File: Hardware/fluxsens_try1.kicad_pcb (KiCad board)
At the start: 2 copper layers, 48.3 x 30.5 mm, 29 parts, among them J1 Conn_Coaxial, J2 Conn_Coaxial, J3 Conn_01x03, U1 DRV5033AJQDBZ, U3 DRV5033AJQDBZ, U5 DRV5033AJQDBZ, U6 DRV5033AJQDBZ

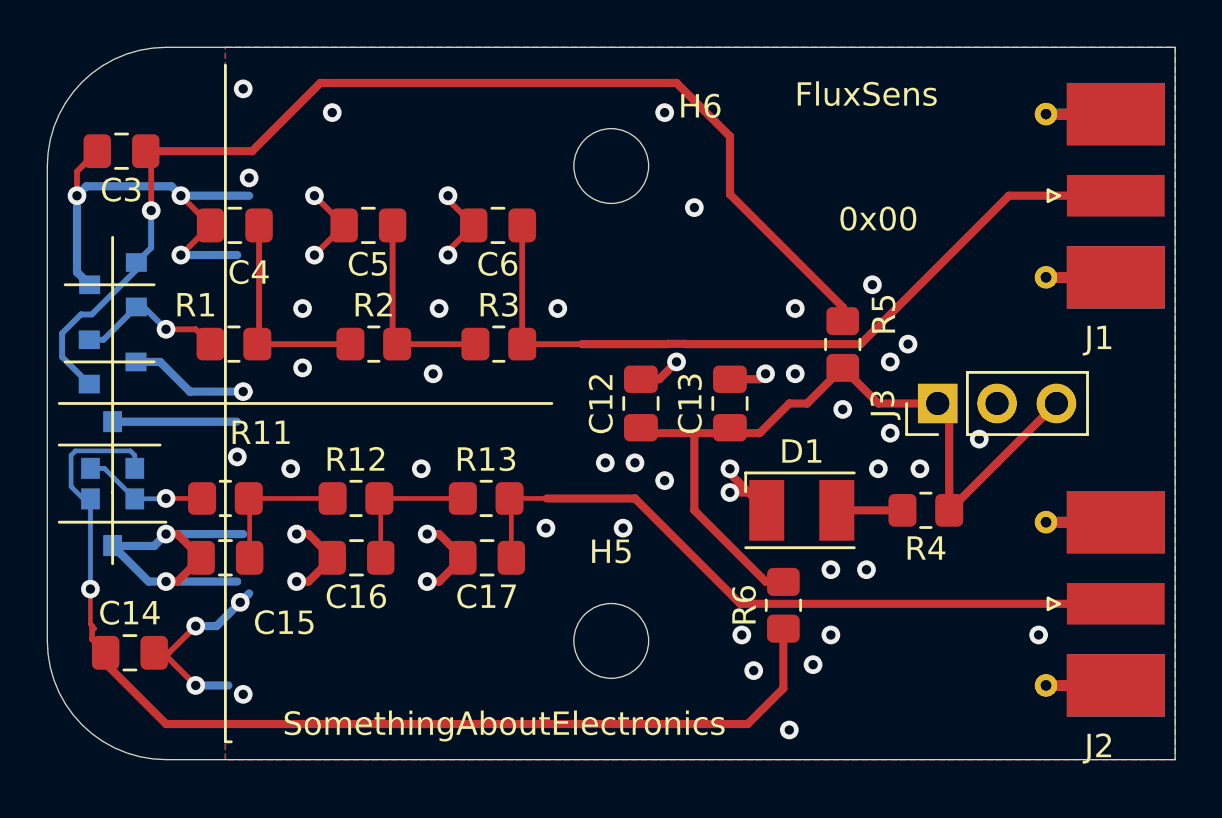
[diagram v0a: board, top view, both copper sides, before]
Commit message: changeover from Kicad V5 to V6
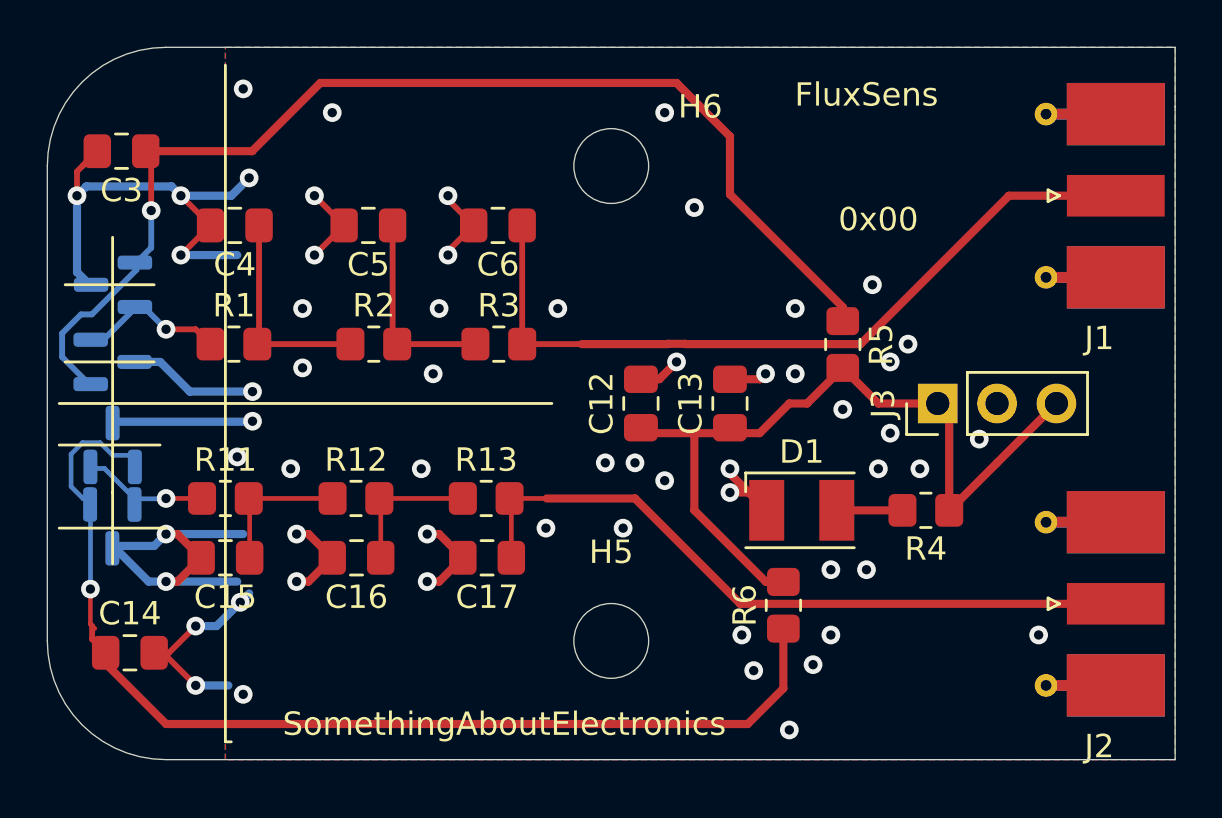
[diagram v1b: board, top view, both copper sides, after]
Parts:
- moved U5 0.18 mm to (48.5, 147.5)
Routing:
- net GND: track 90.6 -> 91.9 mm, vias 58 -> 59
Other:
- net class Default removed
